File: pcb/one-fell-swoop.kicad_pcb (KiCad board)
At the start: 2 copper layers, 107.2 x 86.9 mm, 21 parts, among them J1 MJ-4PP-9, SW1 SW_PUSH, SW10 SW_PUSH, SW11 SW_PUSH, SW12 SW_PUSH, SW13 SW_PUSH, SW14 SW_PUSH, SW15 SW_PUSH, SW16 SW_PUSH, SW17 SW_PUSH, SW2 SW_PUSH, SW3 SW_PUSH, SW4 SW_PUSH, SW5 SW_PUSH, SW6 SW_PUSH, SW7 SW_PUSH, SW8 SW_PUSH, SW9 SW_PUSH, U1 ProMicro

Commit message: Added files for the second version of the Swoop.
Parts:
- removed G***: LOGO, one-fell-swoop:Ferris_rust_logos
- added BT1: Battery, swoop:Battery_pads, F.Cu at (154.0, 118.0)
- added D1: 1N4148W, swoop:D3_SMD, F.Cu at (79.2, 89.2)
- added D10: 1N4148W, swoop:D3_SMD, F.Cu at (135.2, 92.7)
- added D11: 1N4148W, swoop:D3_SMD, F.Cu at (79.2, 123.2)
- added D12: 1N4148W, swoop:D3_SMD, F.Cu at (97.2, 111.2)
- added D13: 1N4148W, swoop:D3_SMD, F.Cu at (115.2, 104.2)
- added D14: 1N4148W, swoop:D3_SMD, F.Cu at (133.2, 109.7)
- added D15: 1N4148W, swoop:D3_SMD, F.Cu at (135.2, 109.7)
- added D16: 1N4148W, swoop:D3_SMD, F.Cu at (142.3, 131.9)
- added D17: 1N4148W, swoop:D3_SMD, F.Cu at (145.8, 133.4)
- added D2: 1N4148W, swoop:D3_SMD, F.Cu at (97.2, 77.2)
- added D3: 1N4148W, swoop:D3_SMD, F.Cu at (115.2, 70.2)
- added D4: 1N4148W, swoop:D3_SMD, F.Cu at (133.2, 75.7)
- added D5: 1N4148W, swoop:D3_SMD, F.Cu at (135.2, 75.7)
- added D6: 1N4148W, swoop:D3_SMD, F.Cu at (79.2, 106.2)
- added D7: 1N4148W, swoop:D3_SMD, F.Cu at (97.2, 94.2)
- added D8: 1N4148W, swoop:D3_SMD, F.Cu at (115.2, 87.2)
- added D9: 1N4148W, swoop:D3_SMD, F.Cu at (133.2, 92.7)
- added ED1: 1N4148W, swoop:D3_SMD, F.Cu at (126.9, 127.8)
- added EN1: RotaryEncoder_Switch, swoop:RotaryEncoder, F.Cu at (115.2, 125.3)
- added EN2: EVQWGD001, swoop:RollerEncoder, F.Cu at (115.2, 125.3)
- added H1: M2 Hole, swoop:M2_hole_4.2mm, F.Cu at (80.2, 83.7)
- added H2: M2 Hole, swoop:M2_hole_4.2mm, F.Cu at (80.2, 112.7)
- added H3: M2 Hole, swoop:M2_hole_4.2mm, F.Cu at (134.2, 82.2)
- added H4: M2 Hole, swoop:M2_hole_4.2mm, F.Cu at (116.2, 110.7)
- added H4: M2 Hole, swoop:M2_hole_4.2mm, F.Cu at (148.5, 121.9)
- added L1: SK6812Mini-e, swoop:SK6812_Mini_E, F.Cu at (71.2, 82.7)
- added L10: SK6812Mini-e, swoop:SK6812_Mini_E, F.Cu at (143.2, 88.7)
- added L11: SK6812Mini-e, swoop:SK6812_Mini_E, F.Cu at (71.2, 116.7)
- added L12: SK6812Mini-e, swoop:SK6812_Mini_E, F.Cu at (89.2, 104.7)
- added L13: SK6812Mini-e, swoop:SK6812_Mini_E, F.Cu at (107.2, 97.7)
- added L14: SK6812Mini-e, jmnw:sk6812_mini_e_rev, F.Cu at (125.2, 103.2)
- added L15: SK6812Mini-e, swoop:SK6812_Mini_E, F.Cu at (143.2, 105.7)
- added L16: SK6812Mini-e, swoop:SK6812_Mini_E, F.Cu at (136.3, 123.5)
- added L17: SK6812Mini-e, swoop:SK6812_Mini_E, F.Cu at (155.9, 131.7)
- added L2: SK6812Mini-e, swoop:SK6812_Mini_E, F.Cu at (89.2, 70.7)
- added L3: SK6812Mini-e, swoop:SK6812_Mini_E, F.Cu at (107.2, 63.7)
- added L4: SK6812Mini-e, swoop:SK6812_Mini_E, F.Cu at (125.2, 69.2)
- added L5: SK6812Mini-e, swoop:SK6812_Mini_E, F.Cu at (143.2, 71.7)
- added L6: SK6812Mini-e, swoop:SK6812_Mini_E, F.Cu at (71.2, 99.7)
- added L7: SK6812Mini-e, swoop:SK6812_Mini_E, F.Cu at (89.2, 87.7)
- added L8: SK6812Mini-e, swoop:SK6812_Mini_E, F.Cu at (107.2, 80.7)
- added L9: SK6812Mini-e, swoop:SK6812_Mini_E, F.Cu at (125.2, 86.2)
- added O1: OLED, swoop:OLED_jumpers, F.Cu at (157.8, 118.7)
- added PSW1: Power, jmnw:Power_reversible, F.Cu at (161.6, 84.0)
- J1: value MJ-4PP-9 -> TRRS; footprint one-fell-swoop:TRRS_jumpers -> swoop:TRRS-3pin
- RSW1: value SW_PUSH -> Reset; footprint one-fell-swoop:Reset_reversible -> swoop:Reset
- SW1, SW10, SW11, SW12, SW13, SW14, SW15, SW2, SW3, SW4, SW5, SW6, SW7, SW8, SW9: value SW_PUSH -> Choc; footprint one-fell-swoop:Choc_reversible -> swoop:Choc
- SW16, SW17: value SW_PUSH -> Choc; footprint one-fell-swoop:Choc_reversible -> swoop:Choc; moved to F.Cu
- U1: footprint one-fell-swoop:ProMicro_jumpers -> swoop:ProMicro_jumpers
- moved SW2 37.6 mm to (89.2, 75.2)
- moved SW7 37.6 mm to (89.2, 92.2)
- moved SW12 37.6 mm to (89.2, 109.2)
- moved SW10 37.5 mm to (143.2, 93.2)
- moved SW13 37.5 mm to (107.2, 102.2)
- moved SW8 37.5 mm to (107.2, 85.2)
- moved SW5 37.5 mm to (143.2, 76.2)
- moved SW15 37.5 mm to (143.2, 110.2)
- moved SW3 37.5 mm to (107.2, 68.2)
- moved SW1 37.5 mm to (71.2, 87.2)
- moved SW6 37.5 mm to (71.2, 104.2)
- moved SW11 37.5 mm to (71.2, 121.2)
- moved SW9 37.5 mm to (125.2, 90.7)
- moved SW4 37.5 mm to (125.2, 73.7)
- moved SW14 37.5 mm to (125.2, 107.7)
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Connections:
- J1 pad A: unconnected-(J1-PadA) -> VCC
- SW1 pad 1: switch1 -> col0
- SW1 pad 2: GND -> Net-(D1-Pad2)
- SW10 pad 1: switch10 -> col4
- SW10 pad 2: GND -> Net-(D10-Pad2)
- SW11 pad 1: switch11 -> col0
- SW11 pad 2: GND -> Net-(D11-Pad2)
- SW12 pad 1: switch12 -> col1
- SW12 pad 2: GND -> Net-(D12-Pad2)
- SW13 pad 1: switch13 -> col2
- SW13 pad 2: GND -> Net-(D13-Pad2)
- SW14 pad 1: switch14 -> col3
- SW14 pad 2: GND -> Net-(D14-Pad2)
- SW15 pad 1: switch15 -> col4
- SW15 pad 2: GND -> Net-(D15-Pad2)
- SW16 pad 1: switch16 -> col3
- SW16 pad 2: GND -> Net-(D16-Pad2)
- SW17 pad 1: switch17 -> col4
- SW17 pad 2: GND -> Net-(D17-Pad2)
- SW2 pad 1: switch2 -> col1
- SW2 pad 2: GND -> Net-(D2-Pad2)
- SW3 pad 1: switch3 -> col2
- SW3 pad 2: GND -> Net-(D3-Pad2)
- SW4 pad 1: switch4 -> col3
- SW4 pad 2: GND -> Net-(D4-Pad2)
- SW5 pad 1: switch5 -> col4
- SW5 pad 2: GND -> Net-(D5-Pad2)
- SW6 pad 1: switch6 -> col0
- SW6 pad 2: GND -> Net-(D6-Pad2)
- SW7 pad 1: switch7 -> col1
- SW7 pad 2: GND -> Net-(D7-Pad2)
- SW8 pad 1: switch8 -> col2
- SW8 pad 2: GND -> Net-(D8-Pad2)
- SW9 pad 1: switch9 -> col3
- SW9 pad 2: GND -> Net-(D9-Pad2)
- U1 pad 1: switch5 -> led
- U1 pad 10: switch8 -> row3
- U1 pad 11: switch7 -> eda
- U1 pad 12: switch6 -> edb
- U1 pad 13: switch17 -> unconnected-(U1-Pad13)
- U1 pad 14: switch16 -> unconnected-(U1-Pad14)
- U1 pad 15: switch11 -> unconnected-(U1-Pad15)
- U1 pad 16: switch12 -> col0
- U1 pad 17: switch13 -> col1
- U1 pad 18: switch14 -> col2
- U1 pad 19: switch15 -> col3
- U1 pad 2: switch4 -> data
- U1 pad 20: data -> col4
- U1 pad 24: unconnected-(U1-Pad24) -> raw
- U1 pad 5: switch3 -> sda
- U1 pad 6: switch2 -> sla
- U1 pad 7: switch1 -> row0
- U1 pad 8: switch10 -> row1
- U1 pad 9: switch9 -> row2
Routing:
- net VCC: track 42.4 -> 402.0 mm, vias 2 -> 6
- net col2: track 0.00 -> 186.5 mm, vias 0 -> 2
- net col0: track 0.00 -> 184.1 mm, vias 0 -> 2
- net col1: track 0.00 -> 160.8 mm, vias 0 -> 2
- net col3: track 0.00 -> 148.7 mm, vias 0 -> 2
- net row0: track 0.00 -> 129.1 mm, vias 0 -> 2
- net col4: track 0.00 -> 123.5 mm, vias 0 -> 1
- net switch1: track 121.2 -> 0.00 mm, vias 1 -> 0
- net switch6: track 116.5 -> 0.00 mm, vias 1 -> 0
- net row1: track 0.00 -> 114.9 mm, vias 0 -> 2
- net switch11: track 112.9 -> 0.00 mm, vias 1 -> 0
- net row2: track 0.00 -> 110.2 mm, vias 0 -> 2
- net switch2: track 96.4 -> 0.00 mm, vias 1 -> 0
- net switch12: track 92.0 -> 0.00 mm, vias 1 -> 0
- net switch7: track 91.6 -> 0.00 mm, vias 1 -> 0
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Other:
- board size 107.2 x 86.9 mm -> 109.3 x 88.7 mm
- board text added: "One Fell Swoop v0.2 https://github.com/jimmerricks/swoop"

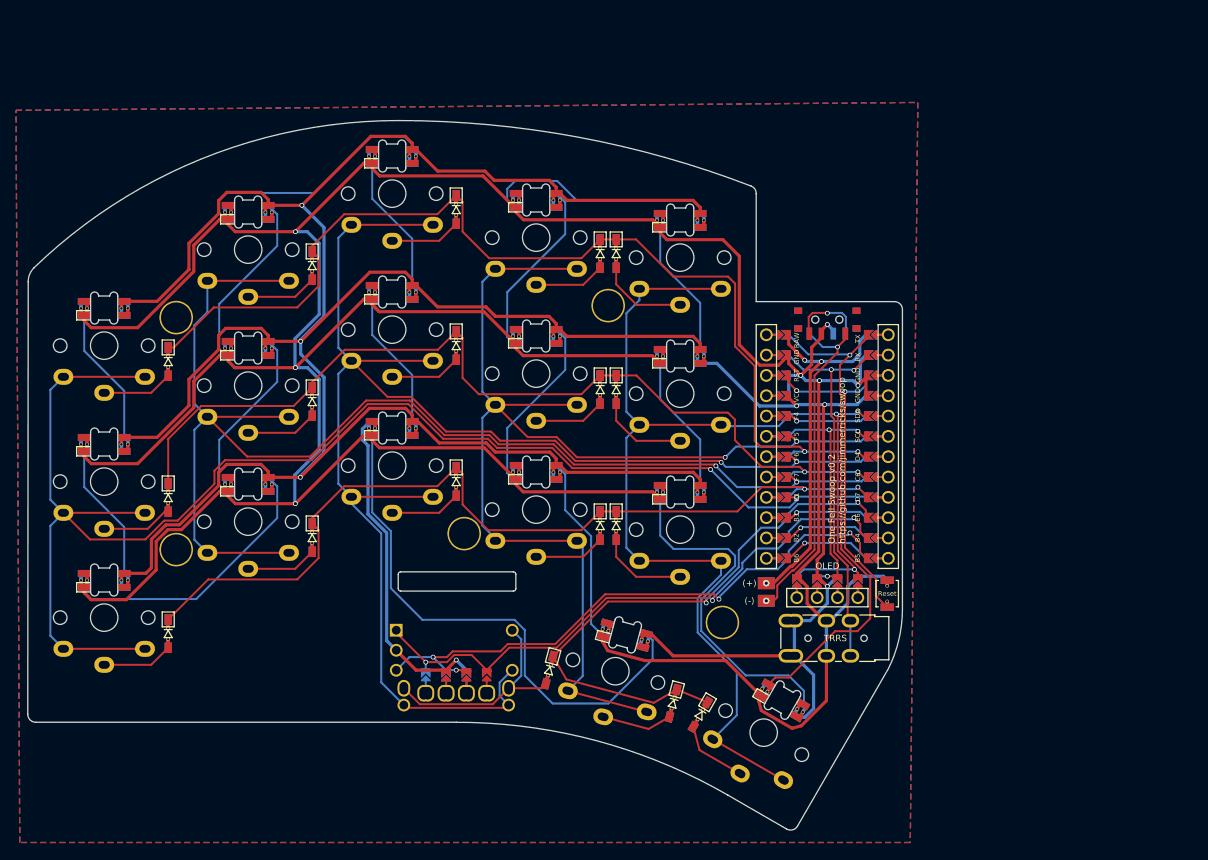
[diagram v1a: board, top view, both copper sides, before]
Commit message: v0.3: fixed route fail, changed shape, added cover
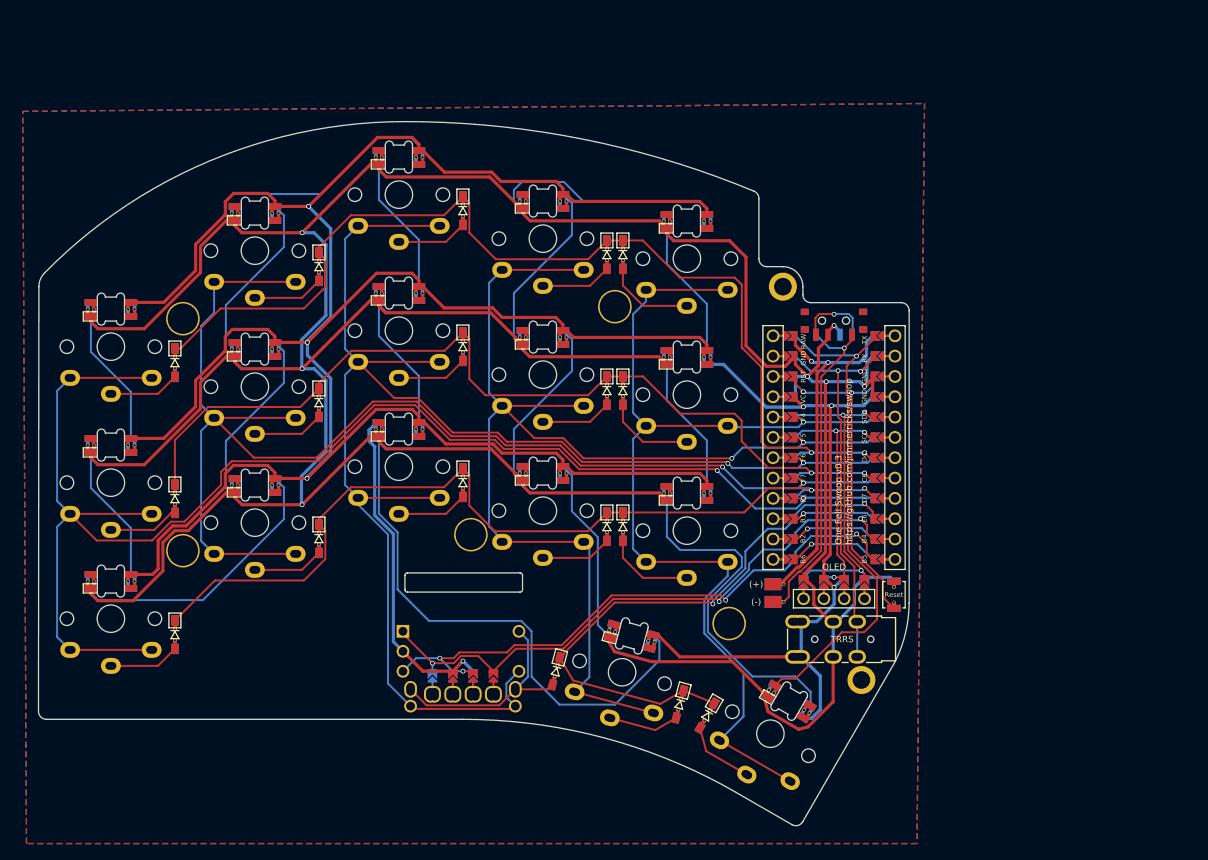
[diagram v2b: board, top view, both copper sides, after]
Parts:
- added Ref**: Val**, jmnw:M2_hole_3.5mm_2mm, F.Cu at (156.1, 79.9)
- added Ref**: Val**, jmnw:M2_hole_3.5mm_2mm, F.Cu at (165.9, 129.0)
- BT1: footprint swoop:Battery_pads -> jmnw:Battery_pads_reversible_2
- L1, L10, L11, L12, L13, L15, L16, L17, L2, L3, L4, L5, L6, L7, L8, L9: footprint swoop:SK6812_Mini_E -> jmnw:sk6812_mini_e_rev
- moved SW12 0.85 mm to (90.1, 109.4)
- moved H2 0.85 mm to (81.1, 112.9)
- moved SW9 0.85 mm to (126.1, 90.9)
- moved D9 0.85 mm to (134.1, 92.9)
- moved L1 0.85 mm to (72.1, 82.8)
- moved D10 0.85 mm to (136.1, 92.9)
- moved D12 0.85 mm to (98.1, 111.4)
- moved H3 0.85 mm to (135.1, 82.4)
- moved BT1 0.85 mm to (154.8, 118.2)
- moved D11 0.85 mm to (80.1, 123.4)
- moved D13 0.85 mm to (116.1, 104.4)
- moved D14 0.85 mm to (134.1, 109.9)
- moved D15 0.85 mm to (136.1, 109.9)
- moved D16 0.85 mm to (143.2, 132.1)
- moved D2 0.85 mm to (98.1, 77.4)
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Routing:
- net Net-(BT1-Pad2): track 42.4 -> 41.3 mm, vias 2 -> 1
- net raw: track 45.3 -> 44.2 mm, vias 3 -> 2
- net col4: track 123.5 -> 124.3 mm
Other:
- board size 109.3 x 88.7 mm -> 108.8 x 88 mm
- board text added: "One Fell Swoop v0.3 https://github.com/jimmerricks/swoop"
- board text removed: "One Fell Swoop v0.2 https://github.com/jimmerricks/swoop"
